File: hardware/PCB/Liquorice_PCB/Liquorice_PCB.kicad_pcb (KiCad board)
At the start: 2 copper layers, 15 parts, among them J1 Conn_01x19_Pin, J2 Conn_01x19_Pin, U1 BMI320, U2 TB6612FNG, U3 XC6206PxxxMR

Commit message: Added BOM and finialized main schematic.
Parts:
- added J3: Conn_01x02_Pin, Connector_PinHeader_2.54mm:PinHeader_1x02_P2.54mm_Vertical, F.Cu at (170.5, 79.0)
- added J4: Conn_01x02_Pin, Connector_PinHeader_2.54mm:PinHeader_1x02_P2.54mm_Vertical, F.Cu at (175.1, 79.0)
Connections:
- net /Motor_Driver/AO1 renamed Net-(J3-Pin_2)
- net /Motor_Driver/AO2 renamed Net-(J3-Pin_1)
- net /Motor_Driver/BO1 renamed Net-(J4-Pin_2)
- net /Motor_Driver/BO2 renamed Net-(J4-Pin_1)
- J1 pad 4: /CS -> /AIN2
- J1 pad 7: unconnected-(J1-Pin_7-Pad7) -> /CS
- J2 pad 13: unconnected-(J2-Pin_13-Pad13) -> /PWMA
- J2 pad 14: unconnected-(J2-Pin_14-Pad14) -> /AIN1
- J2 pad 16: unconnected-(J2-Pin_16-Pad16) -> /BIN1
- J2 pad 8: unconnected-(J2-Pin_8-Pad8) -> /PWMB
- J2 pad 9: unconnected-(J2-Pin_9-Pad9) -> /BIN2
- U2 pad 19: /Motor_Driver/STBY -> VCC

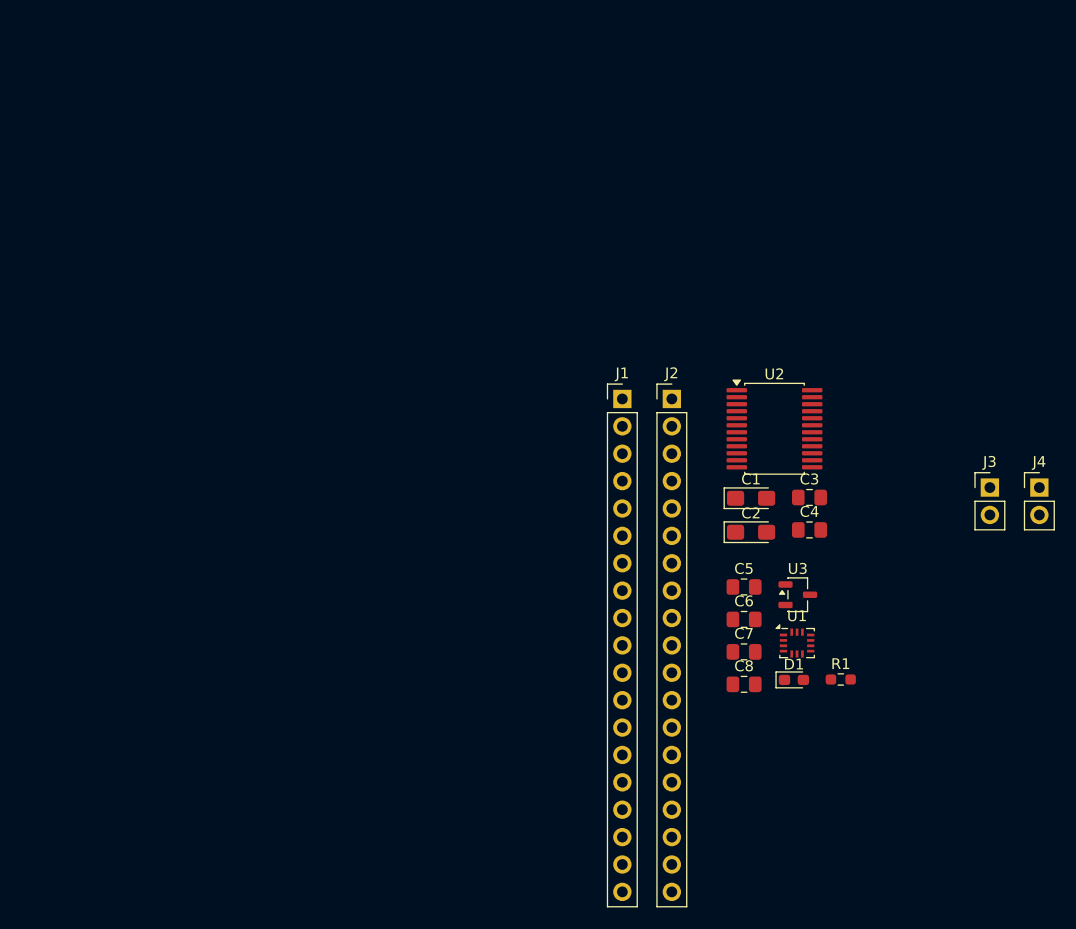
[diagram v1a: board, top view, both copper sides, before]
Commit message: updated readme to contain demo video and future wiring diagram
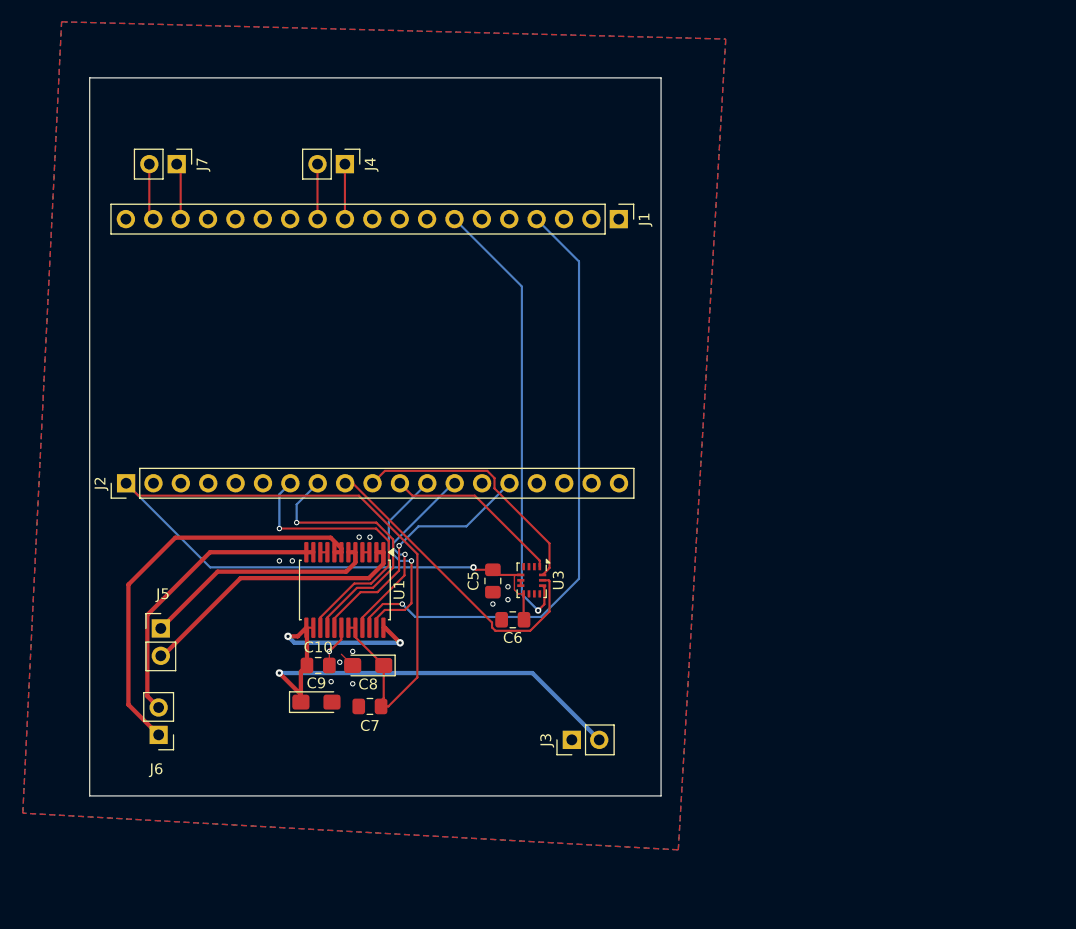
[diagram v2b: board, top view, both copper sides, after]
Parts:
- removed C1, C2: 10uF, Capacitor_Tantalum_SMD:CP_EIA-3216-18_Kemet-A_HandSolder
- removed C3, C4: 100nF, Capacitor_SMD:C_0805_2012Metric_Pad1.18x1.45mm_HandSolder
- removed D1: LED, LED_SMD:LED_0603_1608Metric_Pad1.05x0.95mm_HandSolder
- removed R1: 220, Resistor_SMD:R_0603_1608Metric_Pad0.98x0.95mm_HandSolder
- removed U2: TB6612FNG, Package_SO:SSOP-24_5.3x8.2mm_P0.65mm
- added C10: 100nF, Capacitor_SMD:C_0805_2012Metric_Pad1.18x1.45mm_HandSolder, F.Cu at (108.2, 95.5)
- added C9: 10uF, Capacitor_Tantalum_SMD:CP_EIA-3216-18_Kemet-A_HandSolder, F.Cu at (108.0, 98.9)
- added J5: Conn_01x02_Pin, Connector_PinHeader_2.54mm:PinHeader_1x02_P2.54mm_Vertical, F.Cu at (93.6, 92.1)
- added J6: Conn_01x02_Pin, Connector_PinHeader_2.54mm:PinHeader_1x02_P2.54mm_Vertical, F.Cu at (93.4, 101.9)
- added J7: Conn_01x02_Pin, Connector_PinHeader_2.54mm:PinHeader_1x02_P2.54mm_Vertical, F.Cu at (95.1, 49.0)
- C5: value 10uF -> 100nF
- C8: value 100nF -> 10uF; footprint Capacitor_SMD:C_0805_2012Metric_Pad1.18x1.45mm_HandSolder -> Capacitor_Tantalum_SMD:CP_EIA-3216-18_Kemet-A_HandSolder
- U1: value BMI320 -> TB6612FNG; footprint Package_LGA:Bosch_LGA-14_3x2.5mm_P0.5mm -> Package_SO:SSOP-24_5.3x8.2mm_P0.65mm
- U3: value XC6206PxxxMR -> BMI320; footprint Package_TO_SOT_SMD:SOT-23-3 -> Package_LGA:Bosch_LGA-14_3x2.5mm_P0.5mm
- moved J4 71.1 mm to (110.7, 49.0), turned to -90 degrees
- moved J2 51.2 mm to (90.4, 78.6), turned to 90 degrees
- moved J3 45.3 mm to (131.7, 102.4), turned to 90 degrees
- moved U1 42.2 mm to (110.7, 88.5), turned to -90 degrees
- moved C7 35.1 mm to (113.0, 99.3)
- moved C8 34.9 mm to (112.8, 95.5), turned to 180 degrees
- moved U3 24.7 mm to (128.0, 87.6), turned to -90 degrees
- moved C5 23.3 mm to (124.4, 87.7), turned to -90 degrees
- moved C6 21.5 mm to (126.2, 91.3), turned to 180 degrees
- moved J1 16.7 mm to (136.1, 54.1), turned to -90 degrees
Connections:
- C5 pad 1: GND -> +3.3V
- C5 pad 2: +5V -> GND
- C6 pad 1: GND -> +3.3V
- C6 pad 2: +3.3V -> GND
- C7 pad 1: +3.3V -> GND
- C7 pad 2: GND -> +3.3V
- J1 pad 11: unconnected-(J1-Pin_11-Pad11) -> Net-(J1-Pin_11)
- J1 pad 12: unconnected-(J1-Pin_12-Pad12) -> Net-(J1-Pin_12)
- J1 pad 13: unconnected-(J1-Pin_13-Pad13) -> GND
- J1 pad 17: unconnected-(J1-Pin_17-Pad17) -> Net-(J1-Pin_17)
- J1 pad 18: unconnected-(J1-Pin_18-Pad18) -> Net-(J1-Pin_18)
- J1 pad 19: unconnected-(J1-Pin_19-Pad19) -> GND
- J1 pad 4: /AIN2 -> AIN2
- J1 pad 7: /CS -> CS
- J2 pad 1: unconnected-(J2-Pin_1-Pad1) -> +3.3V
- J2 pad 10: /SCK -> MOSI
- J2 pad 11: /MOSI -> MISO
- J2 pad 12: /MISO -> PWMA
- J2 pad 13: /PWMA -> AIN1
- J2 pad 14: /AIN1 -> GND
- J2 pad 15: unconnected-(J2-Pin_15-Pad15) -> BIN1
- J2 pad 16: /BIN1 -> unconnected-(J2-Pin_16-Pad16)
- J2 pad 19: unconnected-(J2-Pin_19-Pad19) -> VM
- J2 pad 7: unconnected-(J2-Pin_7-Pad7) -> PWMB
- J2 pad 8: /PWMB -> BIN2
- J2 pad 9: /BIN2 -> SCK
- J3 pad 1: Net-(J3-Pin_1) -> GND
- J3 pad 2: Net-(J3-Pin_2) -> VM
- J4 pad 1: Net-(J4-Pin_1) -> Net-(J1-Pin_11)
- J4 pad 2: Net-(J4-Pin_2) -> Net-(J1-Pin_12)
- U1 pad 1: /IMU/MISO -> Net-(J5-Pin_2)
- U1 pad 10: (no net) -> GND
- U1 pad 11: (no net) -> Net-(J6-Pin_2)
- U1 pad 12: /IMU/CS -> Net-(J6-Pin_2)
- U1 pad 13: /IMU/SCK -> VM
- U1 pad 14: /IMU/MOSI -> VM
- U1 pad 2: (no net) -> Net-(J5-Pin_2)
- U1 pad 3: (no net) -> GND
- U1 pad 4: unconnected-(U1-INT1-Pad4) -> GND
- U1 pad 5: +3.3V -> Net-(J5-Pin_1)
- U1 pad 6: GND -> Net-(J5-Pin_1)
- U1 pad 7: GND -> Net-(J6-Pin_1)
- U1 pad 8: +3.3V -> Net-(J6-Pin_1)
- U1 pad 9: unconnected-(U1-INT2-Pad9) -> GND
- U3 pad 1: GND -> MISO
- U3 pad 2: +3.3V -> (no net)
- U3 pad 3: +5V -> (no net)
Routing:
- net +3.3V: track 0.00 -> 100.2 mm, vias 0 -> 1
- net VM: track 0.00 -> 58.4 mm, vias 0 -> 3
- net AIN2: track 0.00 -> 57.9 mm, vias 0 -> 1
- net CS: track 0.00 -> 42.1 mm, vias 0 -> 1
- net Net-(J6-Pin_1): track 0.00 -> 38.1 mm
- net SCK: track 0.00 -> 29.1 mm
- net Net-(J6-Pin_2): track 0.00 -> 26.8 mm
- net PWMB: track 0.00 -> 26.8 mm, vias 0 -> 1
- net Net-(J5-Pin_2): track 0.00 -> 25.9 mm
- net BIN2: track 0.00 -> 25.6 mm, vias 0 -> 1
- net BIN1: track 0.00 -> 23.6 mm, vias 0 -> 1
- net MOSI: track 0.00 -> 23.4 mm
- net Net-(J5-Pin_1): track 0.00 -> 22.2 mm
- net PWMA: track 0.00 -> 18.8 mm, vias 0 -> 1
- net AIN1: track 0.00 -> 18.3 mm, vias 0 -> 1
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- added copper zone on B.Cu, net GND
- added copper zone on F.Cu, net GND
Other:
- board outline added: 53 x 66.6 mm

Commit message: Finalized PCB schematic and layout
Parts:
- added R1: 5.1k, Resistor_SMD:R_0603_1608Metric_Pad0.98x0.95mm_HandSolder, F.Cu at (96.0, 57.8)
- added R2: 5.1k, Resistor_SMD:R_0603_1608Metric_Pad0.98x0.95mm_HandSolder, F.Cu at (99.2, 57.8)
- added R3: 5.1k, Resistor_SMD:R_0603_1608Metric_Pad0.98x0.95mm_HandSolder, F.Cu at (102.4, 57.8)
- added R4: 5.1k, Resistor_SMD:R_0603_1608Metric_Pad0.98x0.95mm_HandSolder, F.Cu at (105.0, 57.8)
- renumbered J3 to J1, J7 to J2, J4 to J3, J5 to J4, J6 to J5, J1 to J6, J2 to J7
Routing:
- net +3.3V: track 100.2 -> 136.9 mm
- net VM: track 58.4 -> 82.9 mm
- net Net-(J3-Pin_2): track 5.10 -> 12.0 mm
- net Net-(J3-Pin_1): track 5.10 -> 11.9 mm
- net Net-(J2-Pin_1): track 5.25 -> 10.2 mm
- net Net-(J2-Pin_2): track 5.25 -> 9.51 mm
- net GND: track 8.32 -> 9.80 mm, vias 12 -> 13
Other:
- board text added: "BATT+"
- board text added: "ENCL"
- board text added: "ENCR"
- board text added: "Liquorice MK1 V1"
- board text added: "Motor L"
- board text added: "Motor R"
- board text added: "SCL"
- board text added: "SDA"

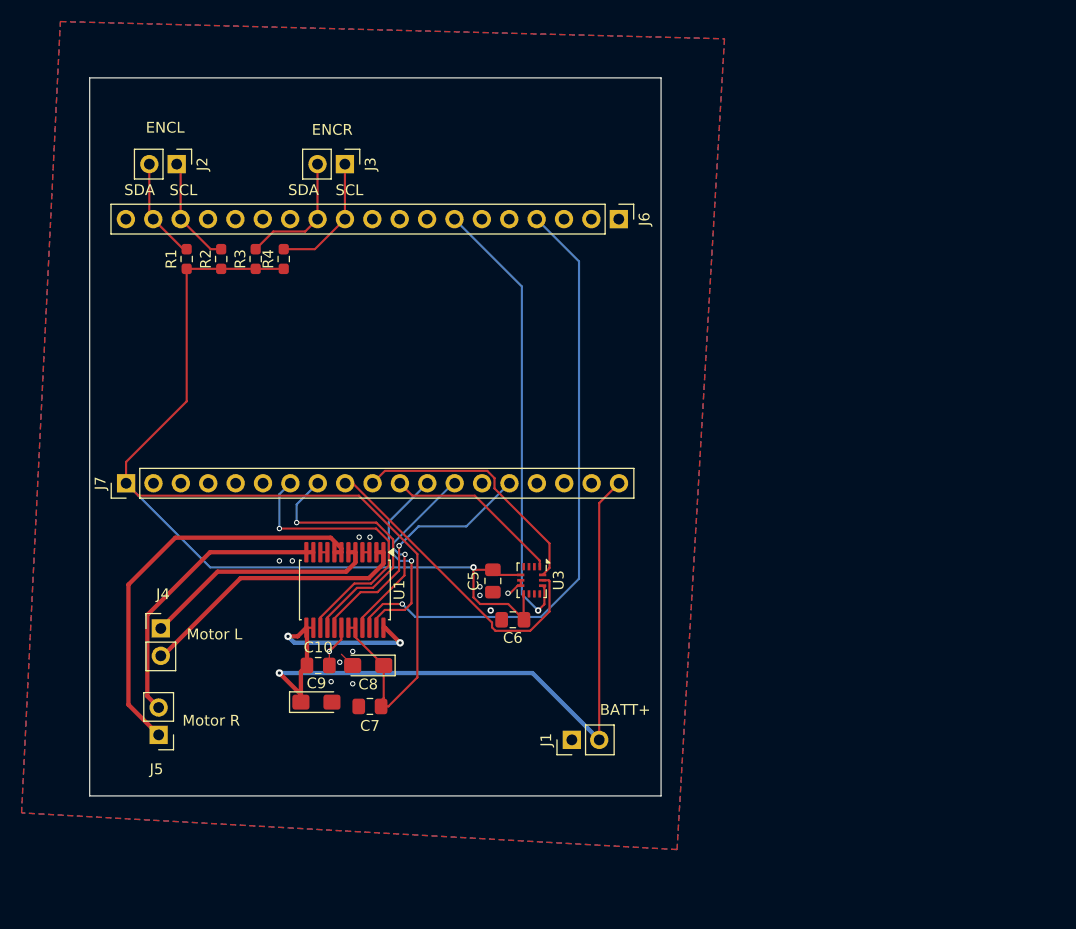
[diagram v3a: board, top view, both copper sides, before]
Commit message: finished PCBs and worked on BOM
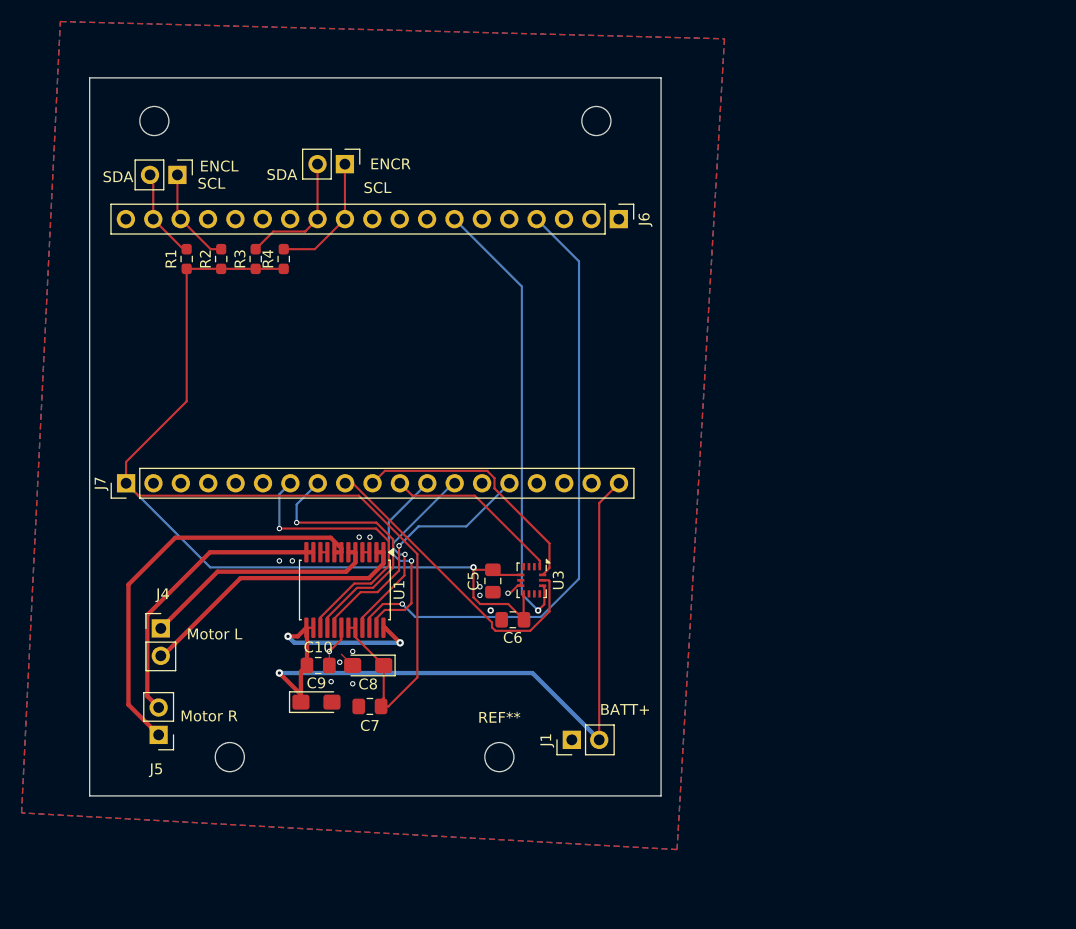
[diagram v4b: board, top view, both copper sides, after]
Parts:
- added REF**: MountingHole_2.7mm_M2.5, MountingHole:MountingHole_2.7mm_M2.5, F.Cu at (125.0, 104.0)
- added REF**: MountingHole_2.7mm_M2.5, MountingHole:MountingHole_2.7mm_M2.5, F.Cu at (134.0, 45.0)
- added REF**: MountingHole_2.7mm_M2.5, MountingHole:MountingHole_2.7mm_M2.5, F.Cu at (93.0, 45.0)
- added REF**: MountingHole_2.7mm_M2.5, MountingHole:MountingHole_2.7mm_M2.5, F.Cu at (100.0, 104.0)
- moved J2 1.00 mm to (95.1, 50.0)
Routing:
- net Net-(J2-Pin_1): track 10.2 -> 9.14 mm
